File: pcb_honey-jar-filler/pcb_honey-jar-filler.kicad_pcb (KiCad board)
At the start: 2 copper layers, 129 x 95.8 mm, 92 parts, among them J1 12V, J12 MOS out (COM, Drain), J13 230V Heater, J14 3V3, J15 5V, J17 GND, J18 GND, J19 Servo, J2 12V, J20 Conn_01x07_Pin, J23 Conn_01x02_Pin, J27 Supply, J28 Relay fallback, J29 Conn_01x02_Pin, J3 3V3, J30 Conn_01x04_Pin, J31 Conn_01x05_Pin, J4 reserve Buttons, J5 4...7V, J6 Conn_01x02_Pin, J7 Conn_01x06_Pin, J8 MOS out (COM, Drain), K6 Relay_LEG-xxF, K7 Relay_LEG-xxF, M2 DC-worm-gear motor (Carousell), Q1 IRLB8721PBF, Q2 IRLB8721PBF, Q6 IRF5305, U1 esp32-devkit-v1_30Pin, U10 LM2576T-ADJ, U3 ULN2003, U4 HX711_24-bit-ADC_weight-scale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, U9 LM2576T-5

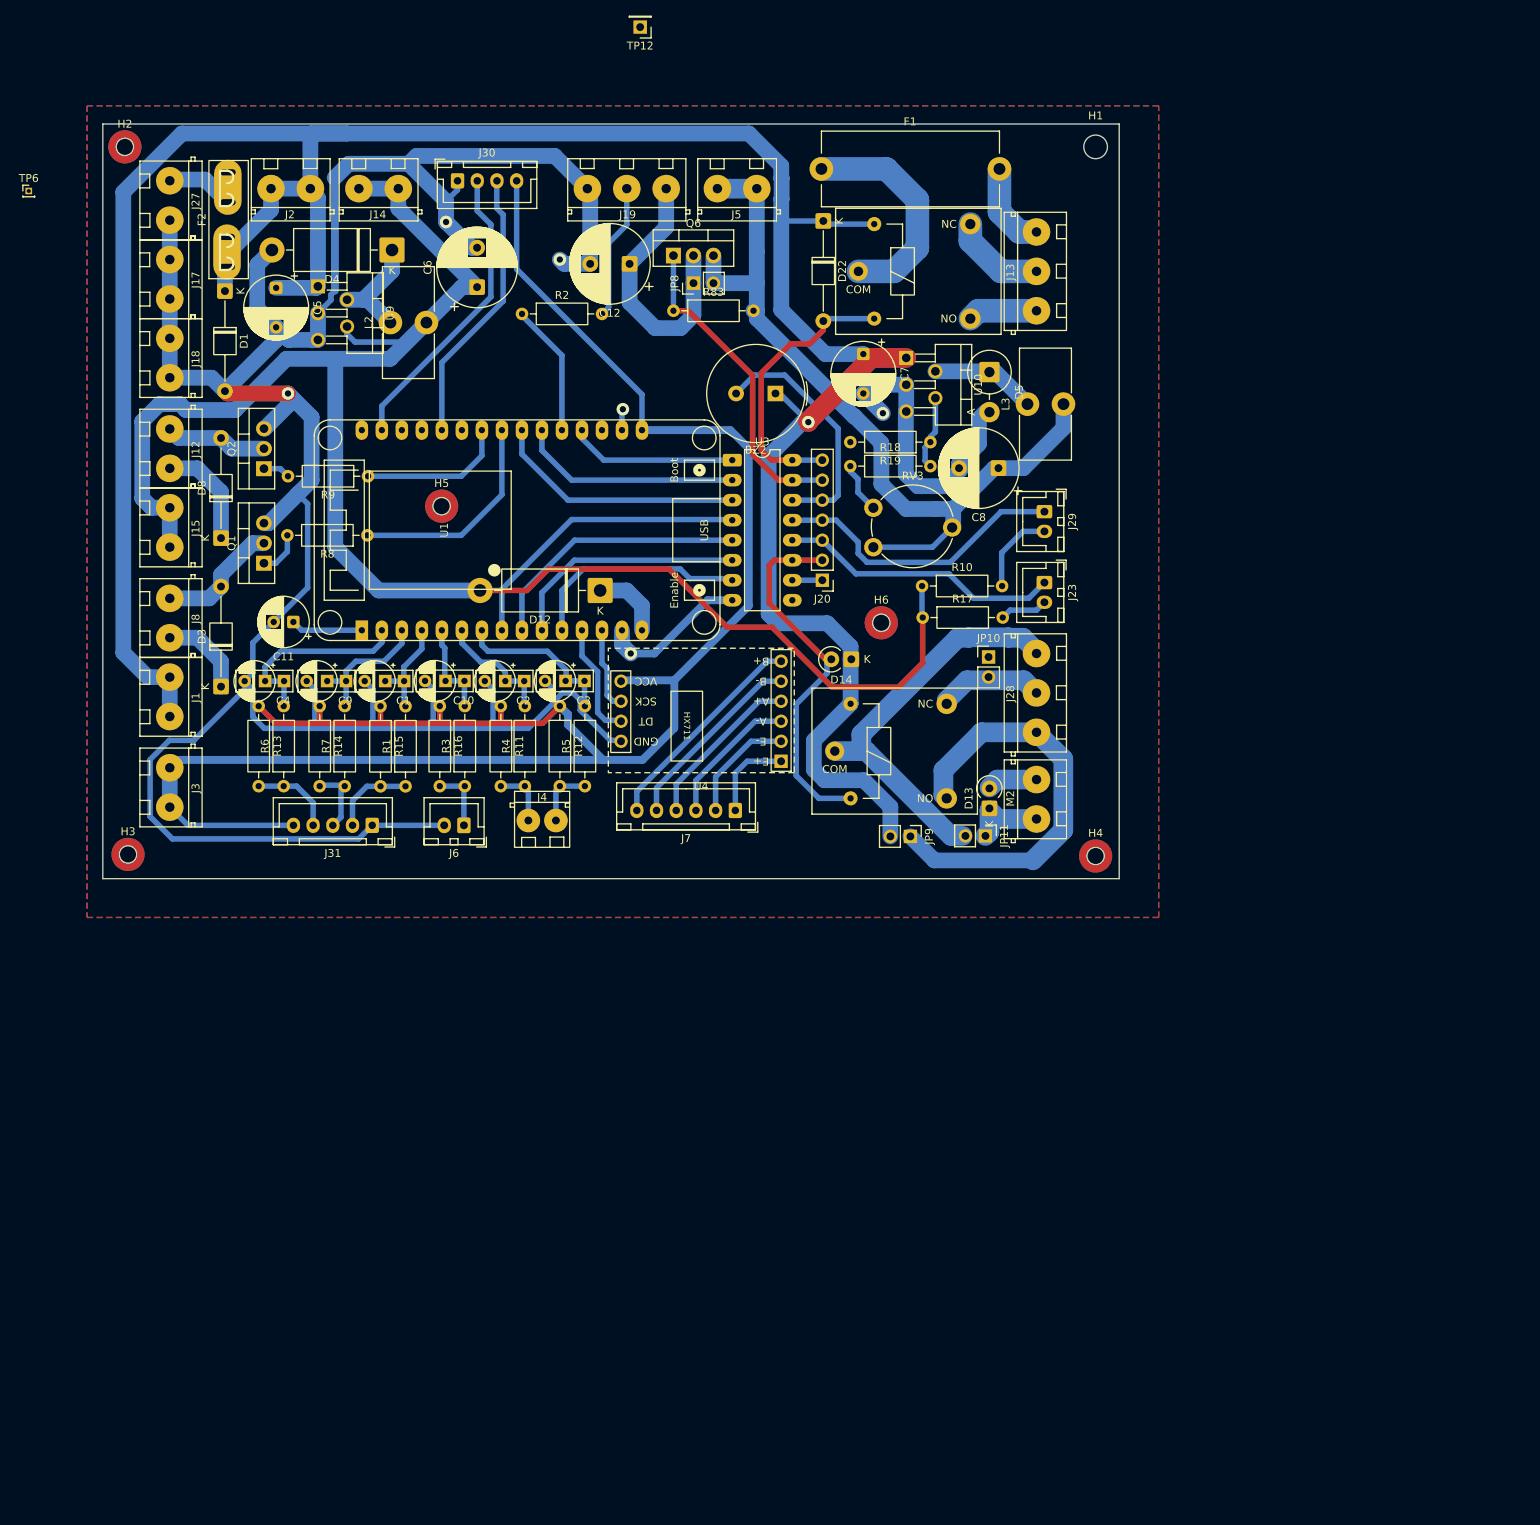
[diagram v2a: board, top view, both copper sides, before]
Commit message: pcb: Add text, testpoints, i2c-pull, Cleanup - DRC-pass
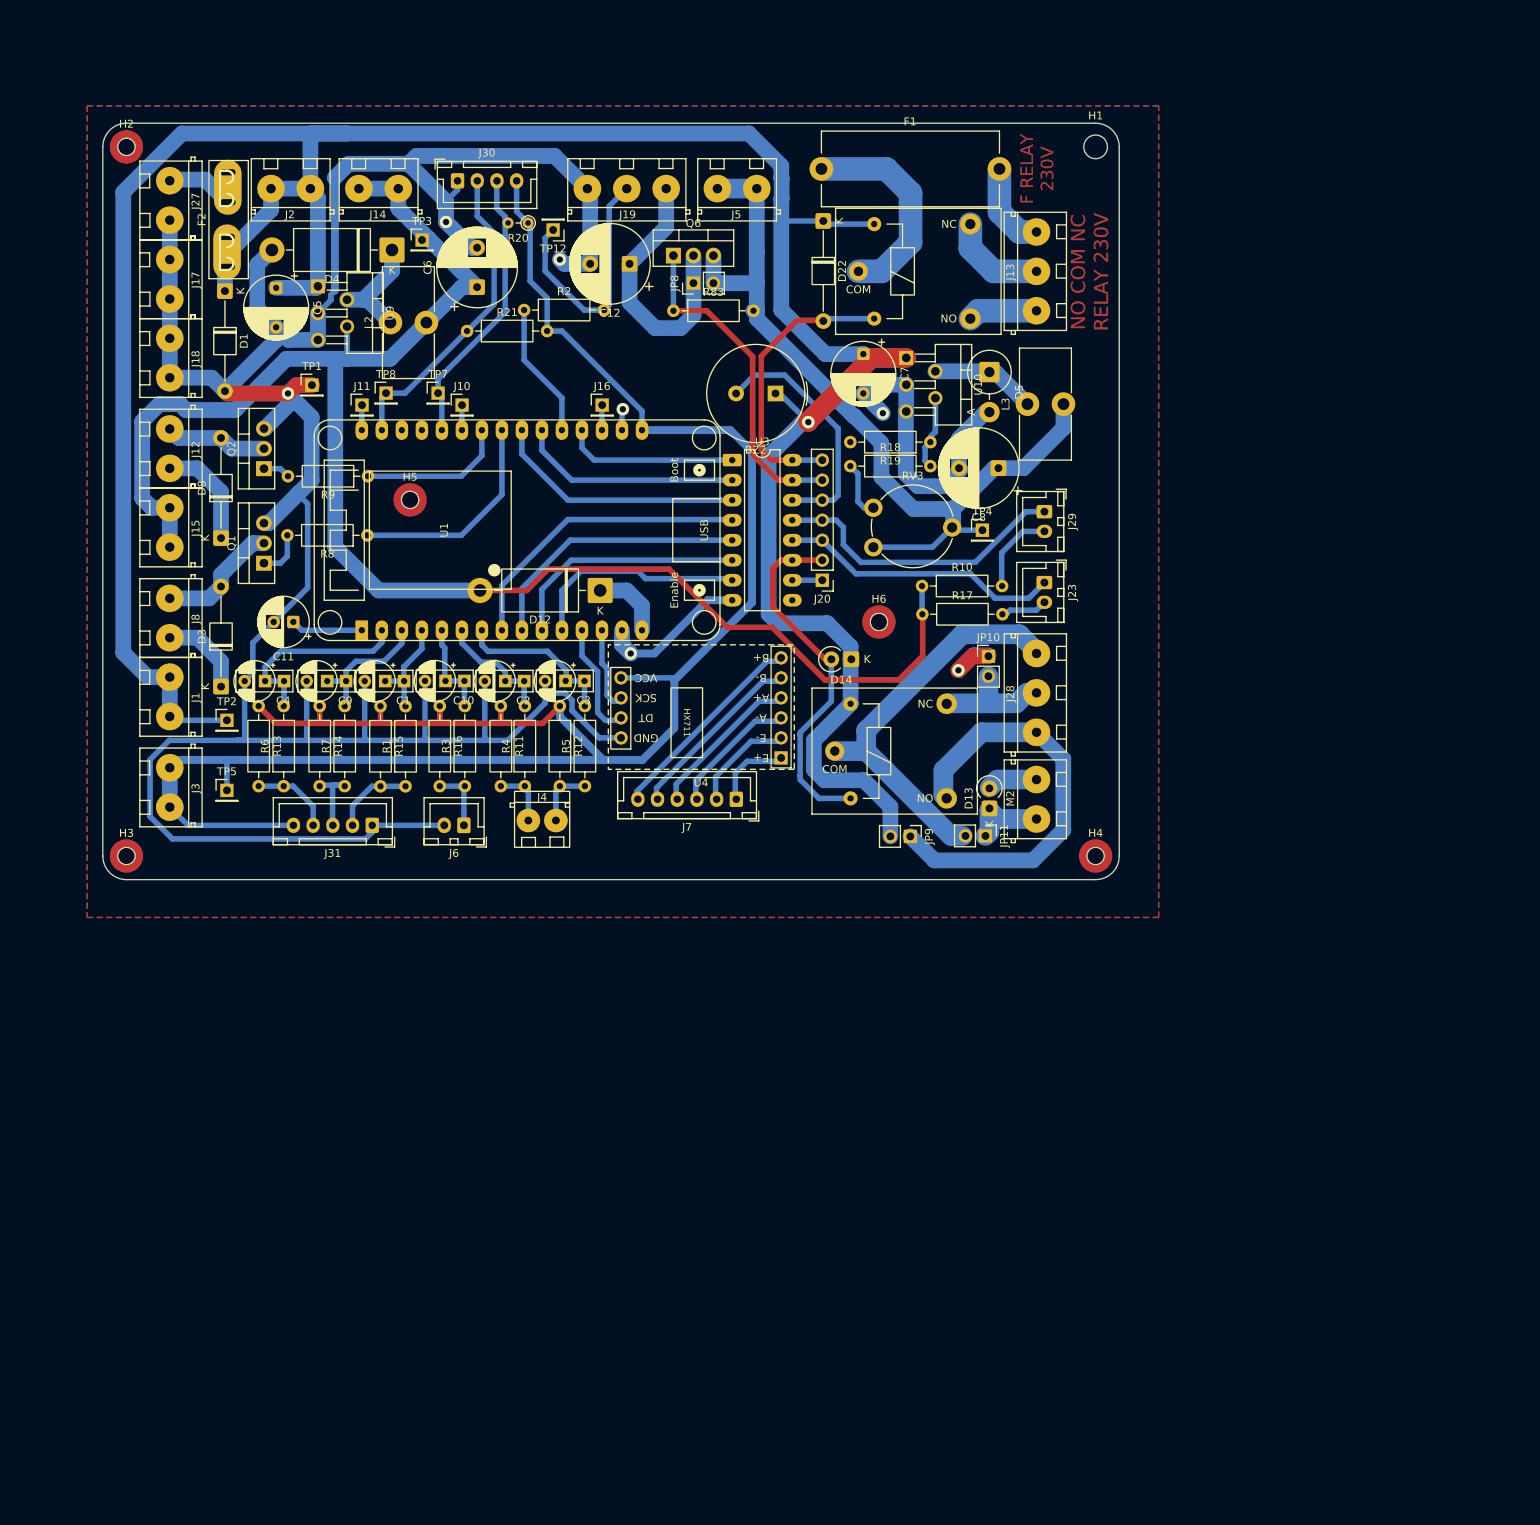
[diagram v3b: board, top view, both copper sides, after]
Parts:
- removed TP6: BATT, Connector_PinHeader_1.00mm:PinHeader_1x01_P1.00mm_Vertical
- added J10: GPIO19, Connector_PinHeader_2.54mm:PinHeader_1x01_P2.54mm_Vertical, F.Cu at (61.6, 54.0)
- added J11: GPIO23, Connector_PinHeader_2.54mm:PinHeader_1x01_P2.54mm_Vertical, F.Cu at (48.9, 54.0)
- added J16: GPIO15, Connector_PinHeader_2.54mm:PinHeader_1x01_P2.54mm_Vertical, F.Cu at (79.4, 54.0)
- added R20: 4k7, Resistor_THT:R_Axial_DIN0204_L3.6mm_D1.6mm_P2.54mm_Vertical, F.Cu at (70.0, 30.9)
- added R21: 4k7, Resistor_THT:R_Axial_DIN0207_L6.3mm_D2.5mm_P10.16mm_Horizontal, F.Cu at (62.2, 44.6)
- added TP1: GND, Connector_PinHeader_2.54mm:PinHeader_1x01_P2.54mm_Vertical, F.Cu at (42.5, 51.4)
- added TP2: 12V, Connector_PinHeader_2.54mm:PinHeader_1x01_P2.54mm_Vertical, F.Cu at (31.8, 94.0)
- added TP3: 5V, Connector_PinHeader_2.54mm:PinHeader_1x01_P2.54mm_Vertical, F.Cu at (56.5, 33.0)
- added TP4: 4-7V, Connector_PinHeader_2.54mm:PinHeader_1x01_P2.54mm_Vertical, F.Cu at (127.6, 69.8)
- added TP5: 3V3, Connector_PinHeader_2.54mm:PinHeader_1x01_P2.54mm_Vertical, F.Cu at (31.8, 102.9)
- added TP7: SDA, Connector_PinHeader_2.54mm:PinHeader_1x01_P2.54mm_Vertical, F.Cu at (58.5, 52.5)
- added TP8: SCL, Connector_PinHeader_2.54mm:PinHeader_1x01_P2.54mm_Vertical, F.Cu at (51.9, 52.5)
- J12: value MOS out (COM, Drain) -> MOS2 out (COM, Drain)
- J14: value 3V3 -> 5V
- J23: value Conn_01x02_Pin -> LED1
- J29: value Conn_01x02_Pin -> LED2
- J30: value Conn_01x04_Pin -> OLED
- J31: value Conn_01x05_Pin -> rotary-encoder
- J6: value Conn_01x02_Pin -> Pos-switch
- J7: value Conn_01x06_Pin -> Bridge (HX711 input)
- J8: value MOS out (COM, Drain) -> MOS1 out (COM, Drain)
- K6, K7: value Relay_LEG-xxF -> Dual Type / universal capacitor footprint
- U1: value esp32-devkit-v1_30Pin -> ESP32-DevKit-V1
- moved TP12 28.0 mm to (73.2, 31.8)
- moved H5 4.08 mm to (55.0, 66.0)
- moved J7 1.42 mm to (96.4, 104.0)
- moved R2 0.56 mm to (69.5, 41.9)
- moved U4 0.43 mm to (91.9, 92.4)
- moved R17 0.42 mm to (120.0, 80.5)
- moved H6 0.32 mm to (114.5, 81.5)
- moved H3 0.28 mm to (19.0, 111.2)
- moved H2 0.20 mm to (19.0, 21.2)
- moved JP10 0.10 mm to (128.4, 85.8)
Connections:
- net /GPIO_Relay-reserve renamed /GPIO_OD-reserve
- net /OD_Relay-reserve renamed /OD_FREE
- U1 pad 18: unconnected-(U1-GPIO15/HSPI_CS/MTDO/[HIGH-AT-BOOT]-Pad18) -> Net-(J16-Pin_1)
- U1 pad 25: unconnected-(U1-GPIO19/VSPI-MISO-Pad25) -> Net-(J10-Pin_1)
- U1 pad 30: unconnected-(U1-GPIO23/VSPI-MOSI-Pad30) -> Net-(J11-Pin_1)
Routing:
- net GND: track 421.9 -> 440.9 mm, vias 6 -> 7
- net Net-(J19-Pin_2): track 17.2 -> 31.8 mm
- net +12V: track 351.4 -> 358.8 mm
- net +3V3: track 244.7 -> 250.1 mm
- net +5V: track 222.4 -> 217.1 mm
- net 4...7V: track 103.7 -> 107.1 mm
- net Net-(J16-Pin_1): track 0.00 -> 3.19 mm
- net Net-(J11-Pin_1): track 0.00 -> 3.19 mm
- net Net-(J10-Pin_1): track 0.00 -> 3.19 mm
- net Net-(J28-Pin_2): track 13.5 -> 15.6 mm
- net /I2C-SCL_OLED: track 38.1 -> 39.8 mm
- net Net-(F1-Pad1): track 28.6 -> 27.0 mm
- net /OD_EN-Servo-pwr: track 41.1 -> 42.5 mm
- net /OD_Relay-motor: track 47.3 -> 46.1 mm
- net Net-(J7-Pin_6): track 27.6 -> 26.4 mm
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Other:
- board size 129 x 95.8 mm -> 129 x 96 mm
- board text added: "+ -"
- board text added: "12V"
- board text added: "12V 12V"
- board text added: "12V GND"
- board text added: "2x-Reserve-IN"
- board text added: "30Pin ESP32-DevkitV1"
- board text added: "3V A B SW GND"
- board text added: "3V SDA SCL GND"
- board text added: "3V3"
- board text added: "3V3 3V3"
- board text added: "4-9V"
- board text added: "4-9V 4-9V"
- board text added: "4-9V PWM GND"
- board text added: "5V"
- board text added: "5V 5V"
- board text added: "7x-OD"
- board text added: "A+ wt"
- board text added: "A- gn"
- board text added: "Adjust 4-9V"
- board text added: "Antenna"
- board text added: "B+ nc"
- board text added: "B- nc"
- board text added: "E+ rd"
- board text added: "E- bk"
- board text added: "EN-Mot"
- board text added: "Encoder"
- board text added: "F 12V"
- board text added: "F RELAY 230V"
- board text added: "FWD Drain"
- board text added: "ForceON"
- board text added: "GND"
- board text added: "GND GND"
- board text added: "GND IN"
- board text added: "HX711 Module"
- board text added: "IO15"
- board text added: "IO19"
- board text added: "IO23"
- board text added: "LED1"
- board text added: "LED2"
- board text added: "MOS1"
- board text added: "MOS2"
- board text added: "Motor"
- board text added: "NO COM NC"
- board text added: "OLED-Display"
- board text added: "PWM"
- board text added: "Pos-switch"
- board text added: "RELAY 230V"
- board text added: "Relay Motor"
- board text added: "SCL"
- board text added: "SDA"
- board text added: "SUPPLY"
- board text added: "Servo"
- board text added: "USB"
- board text added: "pcb-honey-jar-filler V1.0 11.2025"

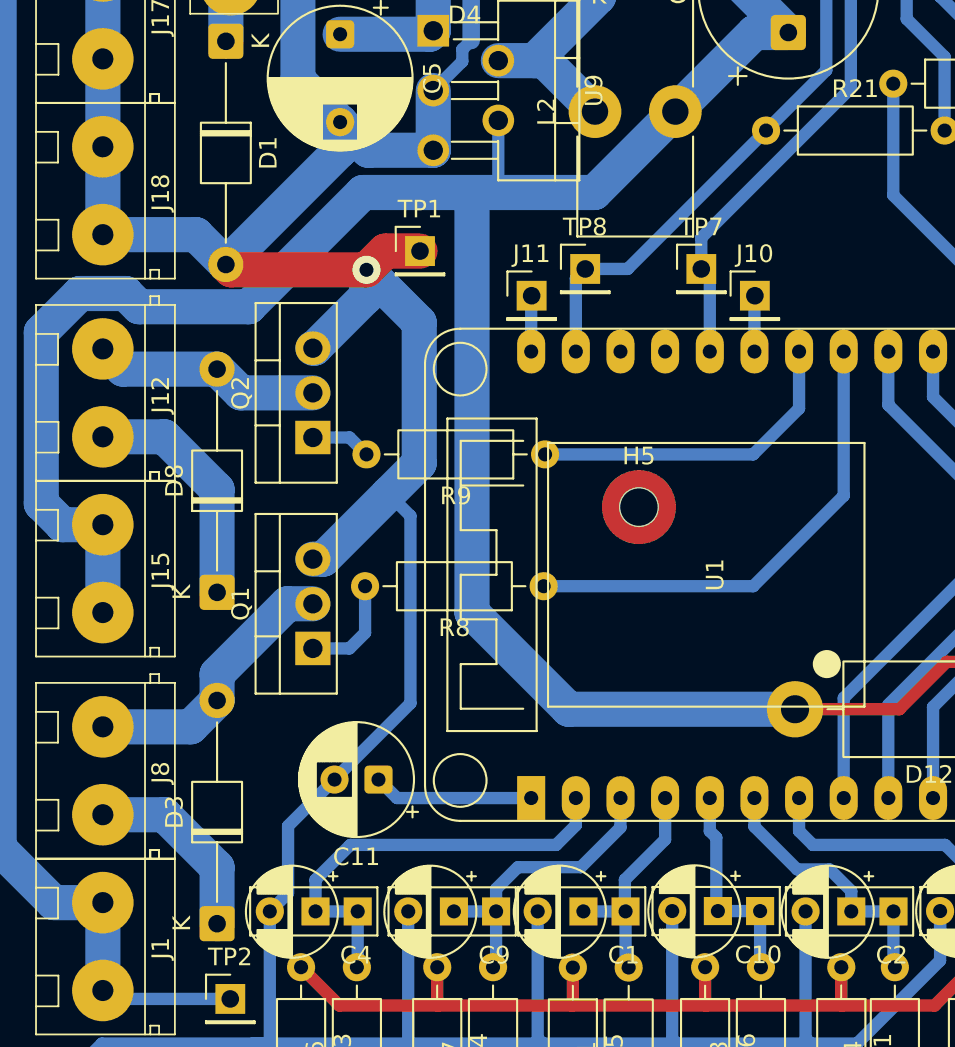
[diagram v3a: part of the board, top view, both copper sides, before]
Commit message: pcb: Add MOS pulldowns, Schematic cleanup
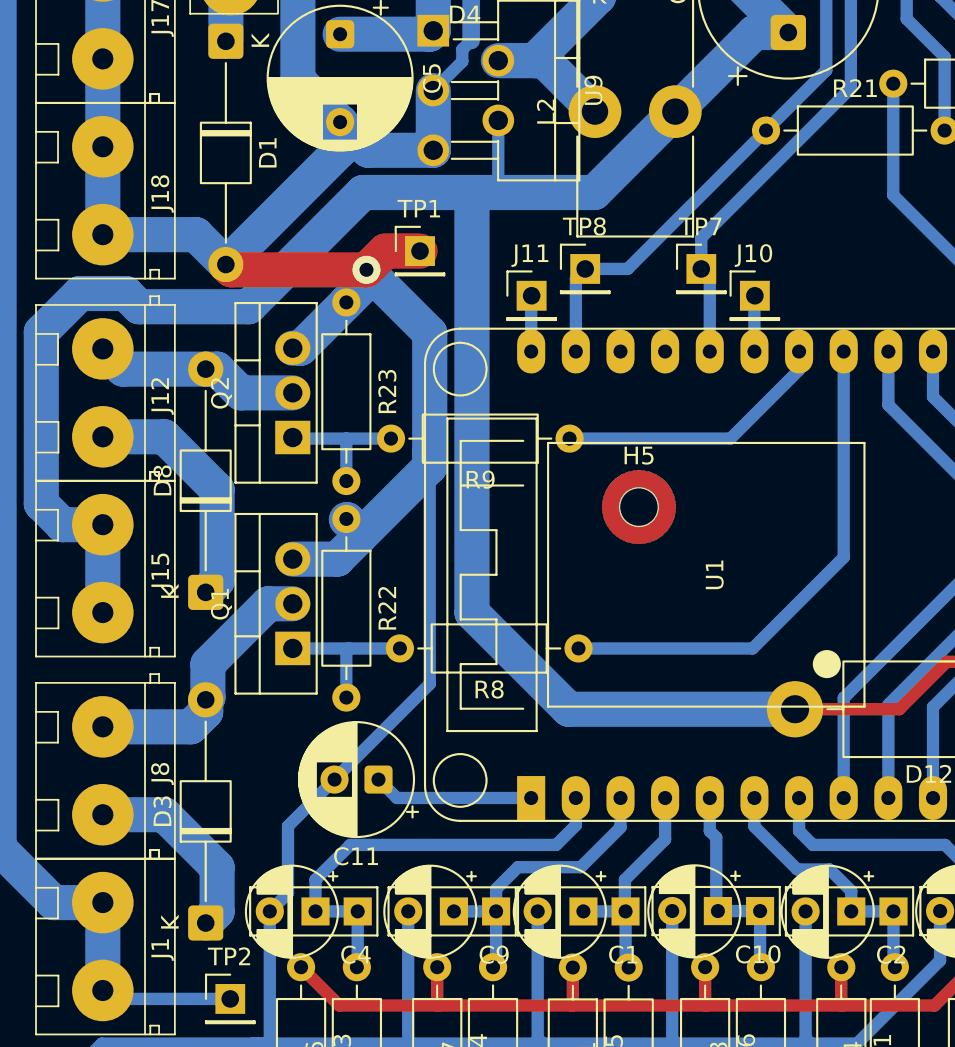
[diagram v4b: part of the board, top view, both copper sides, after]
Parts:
- added R22: 47k, Resistor_THT:R_Axial_DIN0207_L6.3mm_D2.5mm_P10.16mm_Horizontal, F.Cu at (38.4, 66.7)
- added R23: 47k, Resistor_THT:R_Axial_DIN0207_L6.3mm_D2.5mm_P10.16mm_Horizontal, F.Cu at (38.4, 54.4)
- J12: value MOS2 out (COM, Drain) -> MOS2 out (FWD, Drain)
- J7: value Bridge (HX711 input) -> Load-cell (HX711 input)
- J8: value MOS1 out (COM, Drain) -> MOS1 out (FWD, Drain)
- JP10, JP11, JP9: value Jumper_2_Bridged -> EN_motor
- K6, K7: value Dual Type / universal capacitor footprint -> Relay_LEG-xxF
- R10: value 330 -> 220
- U1: value ESP32-DevKit-V1 -> esp32-devkit-v1_30Pin
- moved R8 4.06 mm to (51.6, 74.0)
- moved R9 1.66 mm to (51.1, 62.1)
- moved Q1 1.14 mm to (35.3, 74.0)
- moved Q2 1.14 mm to (35.3, 62.0)
- moved D3 0.65 mm to (30.4, 89.7)
- moved D8 0.65 mm to (30.4, 70.8)
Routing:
- net GND: track 440.9 -> 447.3 mm
- net Net-(Q2-G): track 3.45 -> 8.03 mm
- net +5V: track 217.1 -> 213.6 mm
- net /GPIO_MOS-reserve: track 18.8 -> 15.7 mm
- net Net-(Q1-G): track 5.99 -> 8.94 mm
- net /GPIO_MOS-valve: track 27.4 -> 28.9 mm
- net Net-(D8-A): track 13.0 -> 11.8 mm
- net Net-(D3-A): track 15.7 -> 15.2 mm
